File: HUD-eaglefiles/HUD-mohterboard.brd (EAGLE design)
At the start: 100 x 80 mm, 74 parts, among them U1 LM317, U2 ATMEGA328P_TQFP

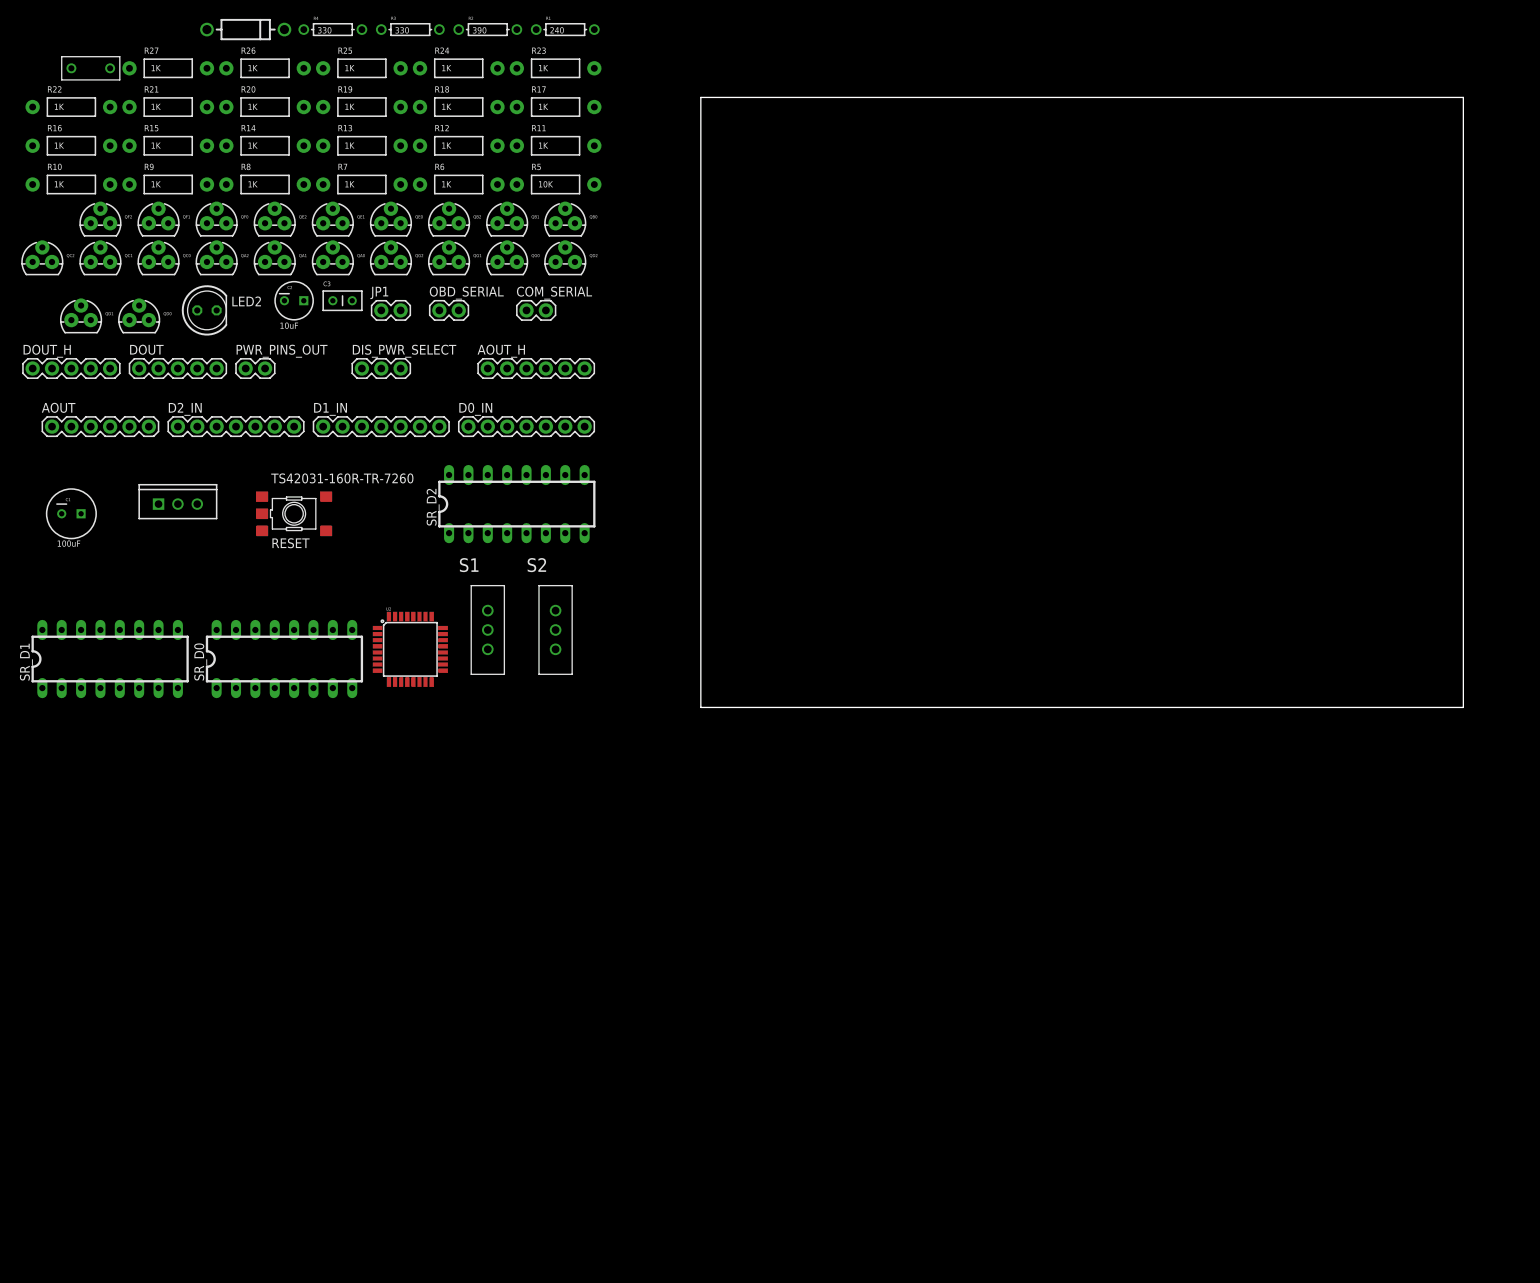
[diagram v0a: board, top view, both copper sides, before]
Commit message: finished the initial matherboard layout and added full layot image
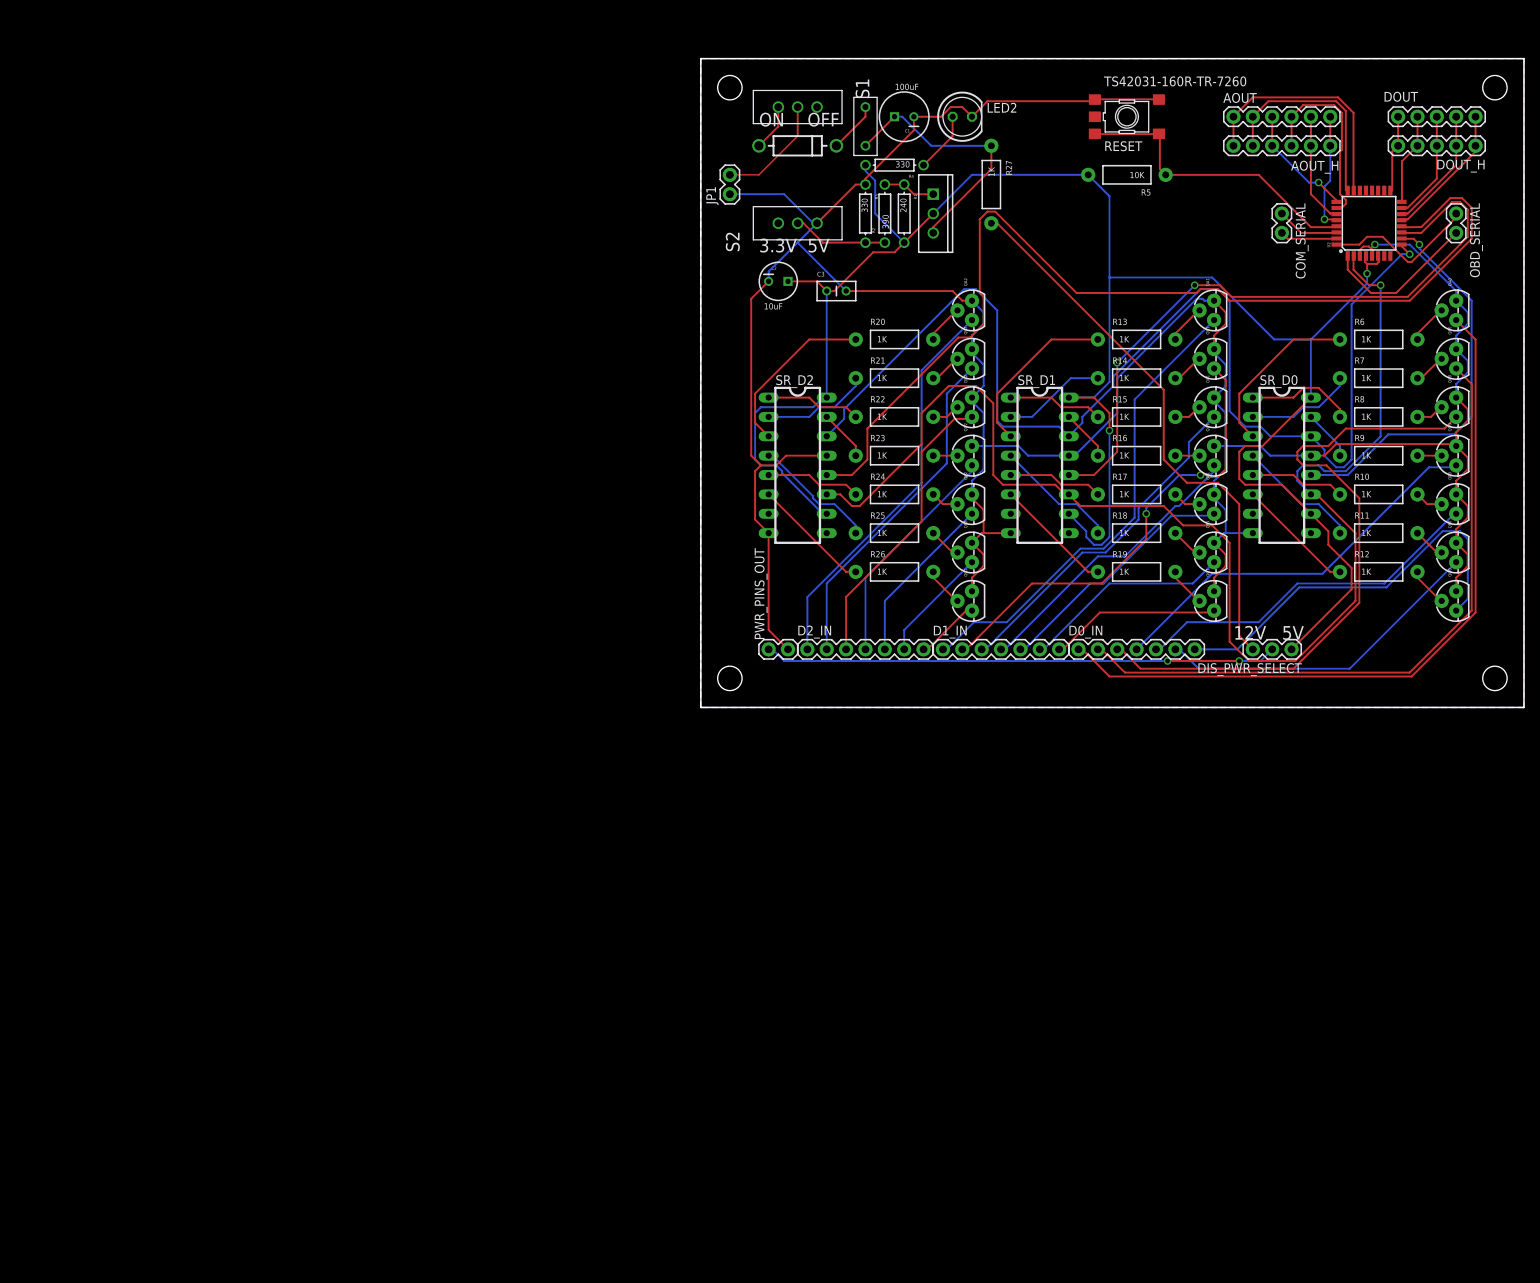
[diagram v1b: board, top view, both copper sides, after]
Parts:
- moved DOUT_H 191.5 mm to (101.6, 73.7), turned to 180 degrees
- moved DOUT 178.3 mm to (101.6, 77.5), turned to 180 degrees
- moved R10 176.2 mm to (88.9, 27.9)
- moved QD0 173.6 mm to (99.1, 33.0), turned to 90 degrees
- moved QC0 171.2 mm to (99.1, 39.4), turned to 90 degrees
- moved QF0 168.2 mm to (99.1, 20.3), turned to 90 degrees
- moved R9 162.7 mm to (88.9, 33.0)
- moved AOUT 160.2 mm to (69.8, 77.5)
- moved QD1 149.6 mm to (67.3, 33.0), turned to 90 degrees
- moved R8 149.2 mm to (88.9, 38.1)
- moved QA0 147.5 mm to (99.1, 52.1), turned to 90 degrees
- moved QC1 147.3 mm to (67.3, 39.4), turned to 90 degrees
- moved R16 145.5 mm to (57.1, 33.0)
- moved QF1 145.0 mm to (67.3, 20.3), turned to 90 degrees
- moved QE0 144.5 mm to (99.1, 26.7), turned to 90 degrees
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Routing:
- net GND: track 0.00 -> 401.6 mm, vias 0 -> 1
- net VCC: track 0.00 -> 270.6 mm, vias 0 -> 2
- net SR_CLK: track 0.00 -> 170.3 mm, vias 0 -> 1
- net SR_SDATA: track 0.00 -> 154.6 mm, vias 0 -> 1
- net CE_D2: track 0.00 -> 134.1 mm
- net N$43: track 0.00 -> 96.4 mm
- net CE_D1: track 0.00 -> 87.7 mm, vias 0 -> 2
- net N$42: track 0.00 -> 86.2 mm
- net N$41: track 0.00 -> 84.1 mm
- net 12VOUT: track 0.00 -> 72.9 mm
- net DISPLAY_PWR-OUT: track 0.00 -> 67.3 mm, vias 0 -> 2
- net N$30: track 0.00 -> 62.5 mm
- net N$29: track 0.00 -> 60.8 mm, vias 0 -> 2
- net N$46: track 0.00 -> 52.7 mm
- net CE_D0: track 0.00 -> 52.3 mm, vias 0 -> 1
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- added copper zone on layer 1, net GND
- added copper zone on layer 16, net GND
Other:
- board size 100 x 80 mm -> 108 x 85.1 mm
- board text added: "12V"
- board text added: "3.3V"
- board text added: "5V"
- board text added: "OFF"
- board text added: "ON"

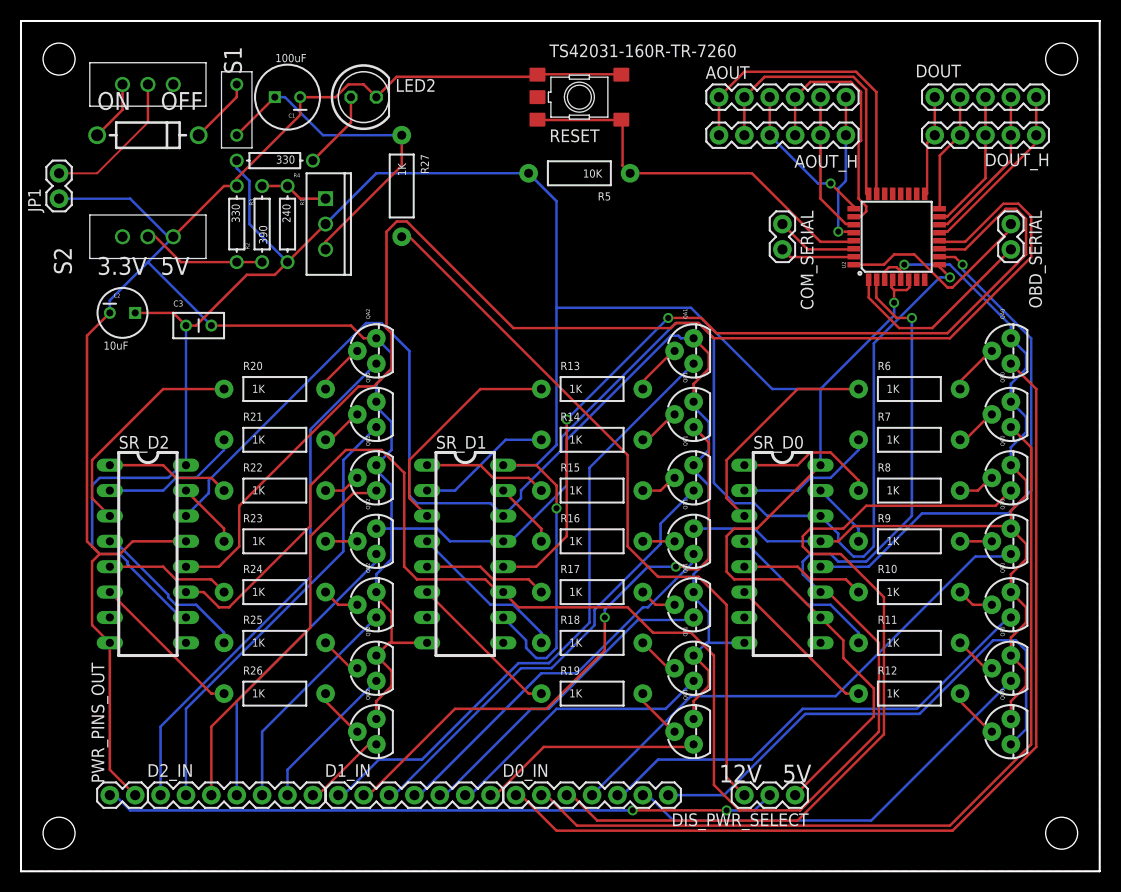
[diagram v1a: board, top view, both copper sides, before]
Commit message: modified the motherboard layout, fixed output pins arrangment and rerout, and added the silk screen text
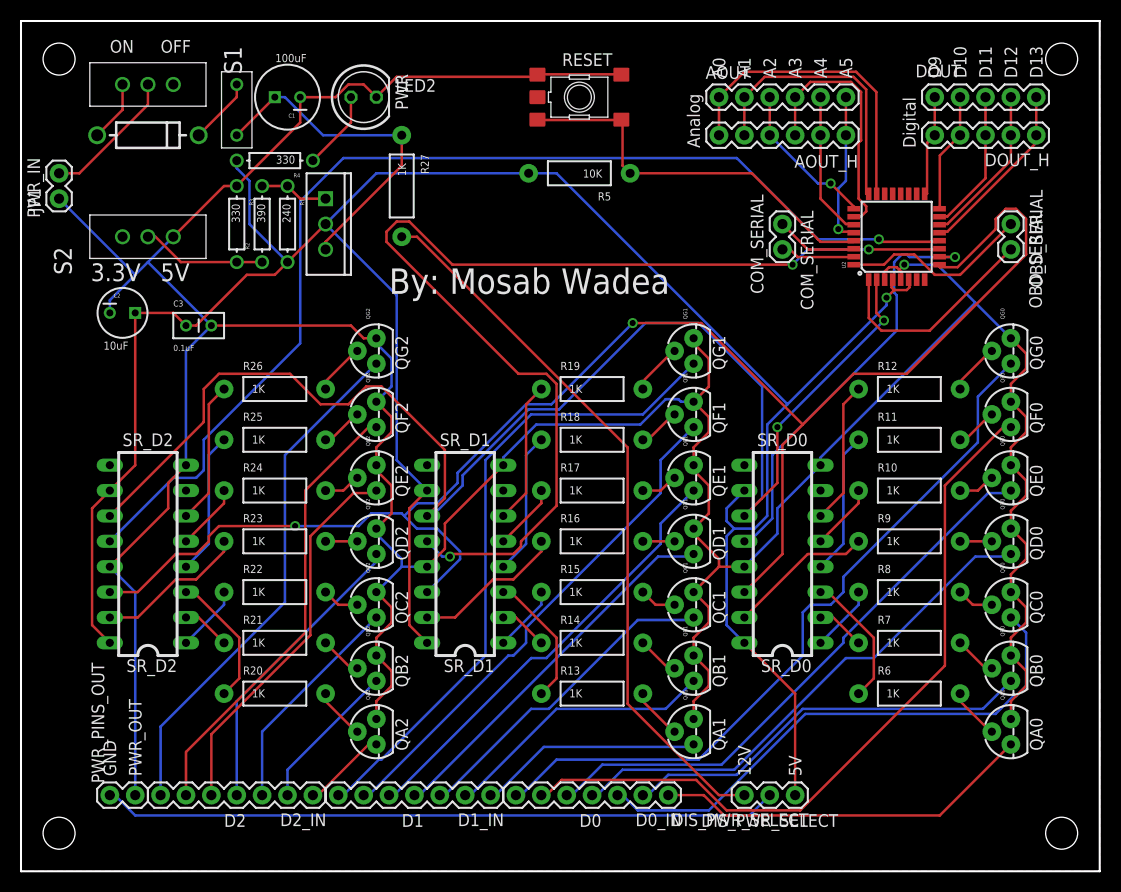
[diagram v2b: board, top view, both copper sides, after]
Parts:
- moved QA0 38.1 mm to (99.1, 14.0)
- moved QA1 38.1 mm to (67.3, 14.0)
- moved QA2 38.1 mm to (35.6, 14.0)
- moved QG0 38.1 mm to (99.1, 52.1)
- moved QG1 38.1 mm to (67.3, 52.1)
- moved QG2 38.1 mm to (35.6, 52.1)
- moved R12 30.5 mm to (88.9, 48.3)
- moved R13 30.5 mm to (57.1, 17.8)
- moved R19 30.5 mm to (57.1, 48.3)
- moved R20 30.5 mm to (25.4, 17.8)
- moved R26 30.5 mm to (25.4, 48.3)
- moved R6 30.5 mm to (88.9, 17.8)
- moved QB0 25.4 mm to (99.1, 20.3)
- moved QB1 25.4 mm to (67.3, 20.3)
- moved QB2 25.4 mm to (35.6, 20.3)
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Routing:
- net N$43: track 96.4 -> 38.1 mm
- net N$42: track 86.2 -> 41.6 mm
- net N$60: track 8.45 -> 52.1 mm
- net N$57: track 52.1 -> 8.45 mm
- net N$33: track 22.4 -> 64.9 mm
- net N$30: track 62.5 -> 22.4 mm
- net N$29: track 60.8 -> 27.6 mm, vias 2 -> 0
- net N$45: track 43.7 -> 75.3 mm
- net N$59: track 15.1 -> 45.2 mm
- net N$41: track 84.1 -> 54.2 mm
- net N$56: track 44.7 -> 15.1 mm
- net SR_CLK: track 170.3 -> 141.5 mm, vias 1 -> 2
- net N$32: track 27.6 -> 51.1 mm
- net VCC: track 270.6 -> 247.2 mm, vias 2 -> 1
- net CE_D1: track 87.7 -> 110.3 mm, vias 2 -> 3
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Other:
- board text added: "A0"
- board text added: "A1"
- board text added: "A2"
- board text added: "A3"
- board text added: "A4"
- board text added: "A5"
- board text added: "Analog"
- board text added: "By: Mosab Wadea"
- board text added: "COM_SERIAL"
- board text added: "D0"
- board text added: "D1"
- board text added: "D10"
- board text added: "D11"
- board text added: "D12"
- board text added: "D13"
- board text added: "D2"
- board text added: "D9"
- board text added: "DIS_PWR_SELECT"
- board text added: "Digital"
- board text added: "GND"
- board text added: "OBD_SERIAL"
- board text added: "PWR"
- board text added: "PWR_IN"
- board text added: "PWR_OUT"
- board text added: "QA0"
- board text added: "QA1"
- board text added: "QA2"
- board text added: "QB0"
- board text added: "QB1"
- board text added: "QB2"
- board text added: "QC0"
- board text added: "QC1"
- board text added: "QC2"
- board text added: "QD0"
- board text added: "QD1"
- board text added: "QD2"
- board text added: "QE0"
- board text added: "QE1"
- board text added: "QE2"
- board text added: "QF0"
- board text added: "QF1"
- board text added: "QF2"
- board text added: "QG0"
- board text added: "QG1"
- board text added: "QG2"
- board text added: "SR_D0"
- board text added: "SR_D1"
- board text added: "SR_D2"

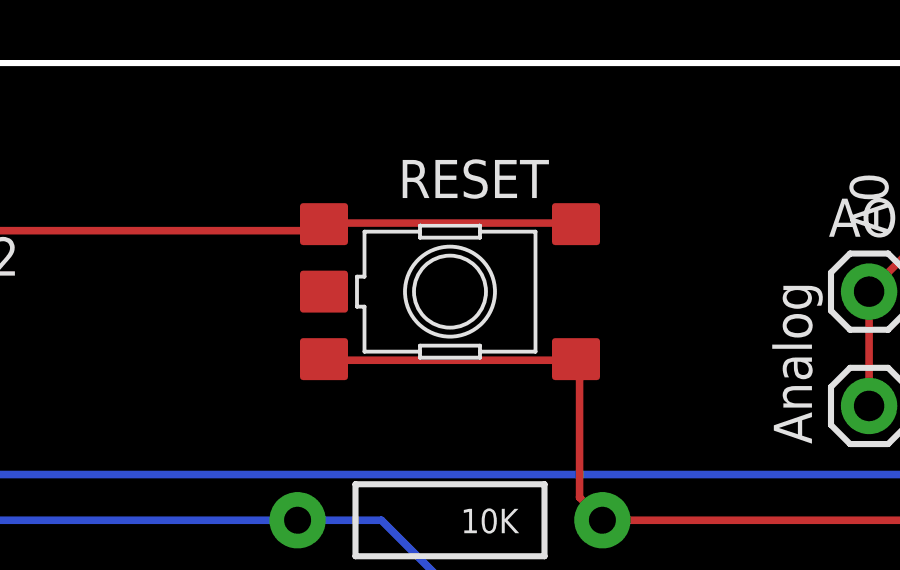
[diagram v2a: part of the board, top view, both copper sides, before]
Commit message: modified the reset button into through hole packaging
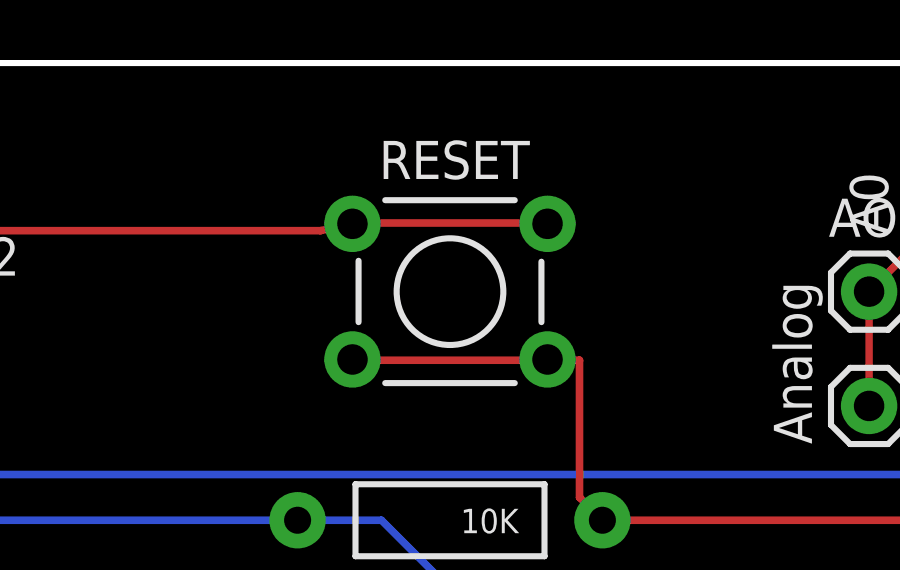
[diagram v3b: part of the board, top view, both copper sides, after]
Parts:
- RESET: device SmartPrj:TS42 -> SparkFun-Retired:TACTILE-PTH
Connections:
- removed net 5-GND: RESET.5
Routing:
- net RESET_WIRE: track 39.5 -> 41.8 mm
- net GND: track 387.0 -> 389.2 mm
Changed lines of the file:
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@@
 <element name="R8" library="SparkFun-Resistors" package="AXIAL-0.4" value="1K" x="88.9" y="27.94"/>
 <element name="R9" library="SparkFun-Resistors" package="AXIAL-0.4" value="1K" x="88.9" y="33.02"/>
-<element name="RESET" library="SmartPrj" package="TS42" value="TS42031-160R-TR-7260" x="55.88" y="77.47" smashed="yes">
-<attribute name="NAME" x="54.15" y="80.59" size="1.27" layer="21"/>
+<element name="RESET" library="SparkFun-Retired" package="TACTILE-PTH" value="TS42031-160R-TR-7260" x="55.88" y="77.47" smashed="yes">
+<attribute name="NAME" x="53.515" y="81.225" size="1.27" layer="21"/>
 </element>
 <element name="S1" library="SparkFun" package="SWITCH-SPST" value="On/Off" x="12.7" y="78.74" rot="R270"/>
@@
 <signals>
 <signal name="5-GND">
-<contactref element="RESET" pad="5"/>
 </signal>
 <signal name="GND">
@@
 <wire x1="8.89" y1="30.48" x2="11.43" y2="27.94" width="0.254" layer="16"/>
 <wire x1="59.944" y1="79.756" x2="51.816" y2="79.756" width="0.254" layer="1"/>
-<wire x1="51.816" y1="79.756" x2="51.68" y2="79.72" width="0.254" layer="1"/>
-<wire x1="59.944" y1="79.756" x2="60.08" y2="79.72" width="0.254" layer="1"/>
+<wire x1="51.816" y1="79.756" x2="52.6288" y2="79.7306" width="0.254" layer="1"/>
+<wire x1="59.944" y1="79.756" x2="59.1312" y2="79.7306" width="0.254" layer="1"/>
 <wire x1="31.496" y1="77.47" x2="27.94" y2="77.47" width="0.254" layer="1"/>
 <wire x1="32.766" y1="78.74" x2="31.496" y2="77.47" width="0.254" layer="1"/>
@@
 <wire x1="37.592" y1="79.502" x2="51.562" y2="79.502" width="0.254" layer="1"/>
 <wire x1="35.56" y1="77.47" x2="37.592" y2="79.502" width="0.254" layer="1"/>
-<wire x1="51.562" y1="79.502" x2="51.68" y2="79.72" width="0.254" layer="1"/>
+<wire x1="51.562" y1="79.502" x2="52.6288" y2="79.7306" width="0.254" layer="1"/>
 <wire x1="8.89" y1="57.15" x2="8.89" y2="55.88" width="0.254" layer="16"/>
 <wire x1="15.24" y1="63.5" x2="12.7" y2="60.96" width="0.254" layer="16"/>
@@
 <contactref element="R5" pad="P$1"/>
 <wire x1="59.944" y1="75.184" x2="51.816" y2="75.184" width="0.254" layer="1"/>
-<wire x1="51.816" y1="75.184" x2="51.68" y2="75.22" width="0.254" layer="1"/>
-<wire x1="59.944" y1="75.184" x2="60.08" y2="75.22" width="0.254" layer="1"/>
+<wire x1="51.816" y1="75.184" x2="52.6288" y2="75.2094" width="0.254" layer="1"/>
+<wire x1="59.944" y1="75.184" x2="59.1312" y2="75.2094" width="0.254" layer="1"/>
 <wire x1="80.01" y1="62.992" x2="83.312" y2="62.992" width="0.254" layer="1"/>
 <wire x1="73.152" y1="69.85" x2="80.01" y2="62.992" width="0.254" layer="1"/>
@@
 <wire x1="60.198" y1="70.612" x2="60.198" y2="75.184" width="0.254" layer="1"/>
 <wire x1="60.96" y1="69.85" x2="60.198" y2="70.612" width="0.254" layer="1"/>
-<wire x1="60.198" y1="75.184" x2="60.08" y2="75.22" width="0.254" layer="1"/>
+<wire x1="60.198" y1="75.184" x2="59.1312" y2="75.2094" width="0.254" layer="1"/>
 </signal>
 <signal name="N$6">
